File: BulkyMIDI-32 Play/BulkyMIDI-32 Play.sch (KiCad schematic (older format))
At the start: 45 parts, among them IC1 0.91_I2C_OLED, J1 DC IN, J10 MIDI IN (ALT), J11 MIDI OUT (ALT), J2 MIDI OUT, J3 MIDI IN, J4 Conn_Power, J5 MIDI THRU, J6 Play_Panel, M1 Mounting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

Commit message: Add schematic notes
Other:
- note added: "For a basic device with only MIDI OUT, the remaining\nMIDI components can be omitted. When building only\none MIDI IN circuit, you need to add R7 from the\nalternate circuit as well to avoid floating gate inputs."
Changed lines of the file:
@@
 Wire Bus Line
 	15050 7275 15050 8950
+Text Notes 9775 7375 0    50   ~ 0
+For a basic device with only MIDI OUT, the remaining\nMIDI components can be omitted. When building only\none MIDI IN circuit, you need to add R7 from the\nalternate circuit as well to avoid floating gate inputs.
 $EndSCHEMATC

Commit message: Build tweaks
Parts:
- U1: footprint Package_DIP:DIP-14_W7.62mm -> Package_DIP:DIP-14_W7.62mm_Socket_LongPads
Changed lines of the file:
@@
 F 0 "U1" H 6025 5775 50  0000 C CNN
 F 1 "74HCT14" H 6025 5700 50  0000 C CNN
-F 2 "Package_DIP:DIP-14_W7.62mm" H 6025 5500 50  0001 C CNN
+F 2 "Package_DIP:DIP-14_W7.62mm_Socket_LongPads" H 6025 5500 50  0001 C CNN
 F 3 "http://www.ti.com/lit/gpn/sn74HC14" H 6025 5500 50  0001 C CNN
 	4    6025 5500
@@
 F 0 "U1" H 5275 5875 50  0000 C CNN
 F 1 "74HCT14" H 5275 5800 50  0000 C CNN
-F 2 "Package_DIP:DIP-14_W7.62mm" H 5275 6050 50  0001 C CNN
+F 2 "Package_DIP:DIP-14_W7.62mm_Socket_LongPads" H 5275 6050 50  0001 C CNN
 F 3 "http://www.ti.com/lit/gpn/sn74HC14" H 5275 6050 50  0001 C CNN
 	5    5275 6050
@@
 F 0 "U1" H 6025 5875 50  0000 C CNN
 F 1 "74HCT14" H 6025 5800 50  0000 C CNN
-F 2 "Package_DIP:DIP-14_W7.62mm" H 6025 6050 50  0001 C CNN
+F 2 "Package_DIP:DIP-14_W7.62mm_Socket_LongPads" H 6025 6050 50  0001 C CNN
 F 3 "http://www.ti.com/lit/gpn/sn74HC14" H 6025 6050 50  0001 C CNN
 	6    6025 6050
@@
 F 0 "U1" V 10883 10250 50  0000 C CNN
 F 1 "74HCT14" V 10974 10250 50  0000 C CNN
-F 2 "Package_DIP:DIP-14_W7.62mm" H 11250 10250 50  0001 C CNN
+F 2 "Package_DIP:DIP-14_W7.62mm_Socket_LongPads" H 11250 10250 50  0001 C CNN
 F 3 "http://www.ti.com/lit/gpn/sn74HC14" H 11250 10250 50  0001 C CNN
 	7    11250 10250
@@
 F 0 "U1" H 6025 7300 50  0000 C CNN
 F 1 "74HCT14" H 6025 7225 50  0000 C CNN
-F 2 "Package_DIP:DIP-14_W7.62mm" H 6025 7475 50  0001 C CNN
+F 2 "Package_DIP:DIP-14_W7.62mm_Socket_LongPads" H 6025 7475 50  0001 C CNN
 F 3 "http://www.ti.com/lit/gpn/sn74HC14" H 6025 7475 50  0001 C CNN
 	2    6025 7475
@@
 F 0 "U1" H 5275 7300 50  0000 C CNN
 F 1 "74HCT14" H 5275 7225 50  0000 C CNN
-F 2 "Package_DIP:DIP-14_W7.62mm" H 5275 7475 50  0001 C CNN
+F 2 "Package_DIP:DIP-14_W7.62mm_Socket_LongPads" H 5275 7475 50  0001 C CNN
 F 3 "http://www.ti.com/lit/gpn/sn74HC14" H 5275 7475 50  0001 C CNN
 	1    5275 7475
@@
 Wire Wire Line
 	8050 7475 8125 7475
+Text Notes 9775 7375 0    50   ~ 0
+For a basic device with only MIDI OUT, the remaining\nMIDI components can be omitted. When building only\none MIDI IN circuit, you need to add R7 from the\nalternate circuit as well to avoid floating gate inputs.
 Wire Bus Line
 	15050 1100 15050 1275
@@
 Wire Bus Line
 	15050 7275 15050 8950
-Text Notes 9775 7375 0    50   ~ 0
-For a basic device with only MIDI OUT, the remaining\nMIDI components can be omitted. When building only\none MIDI IN circuit, you need to add R7 from the\nalternate circuit as well to avoid floating gate inputs.
 $EndSCHEMATC

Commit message: Forgotten gate
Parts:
- added unit 3 of U1
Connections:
- net GND: now also U1.5
- no-connect marks 18 -> 19
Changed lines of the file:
@@
 Text Notes 9775 7375 0    50   ~ 0
 For a basic device with only MIDI OUT, the remaining\nMIDI components can be omitted. When building only\none MIDI IN circuit, you need to add R7 from the\nalternate circuit as well to avoid floating gate inputs.
+$Comp
+L 74xx:74HC14 U1
+U 3 1 62B9B026
+P 6825 10600
+F 0 "U1" H 6825 10425 50  0000 C CNN
+F 1 "74HCT14" H 6825 10350 50  0000 C CNN
+F 2 "Package_DIP:DIP-14_W7.62mm_Socket_LongPads" H 6825 10600 50  0001 C CNN
+F 3 "http://www.ti.com/lit/gpn/sn74HC14" H 6825 10600 50  0001 C CNN
+	3    6825 10600
+	0    -1   -1   0
+$EndComp
+NoConn ~ 6825 10300
+$Comp
+L power:GND #PWR0121
+U 1 1 62BAE7B4
+P 6825 10900
+F 0 "#PWR0121" H 6825 10650 50  0001 C CNN
+F 1 "GND" H 6830 10727 50  0000 C CNN
+F 2 "" H 6825 10900 50  0001 C CNN
+F 3 "" H 6825 10900 50  0001 C CNN
+	1    6825 10900
+	1    0    0    -1
+$EndComp
 Wire Bus Line
 	15050 1100 15050 1275

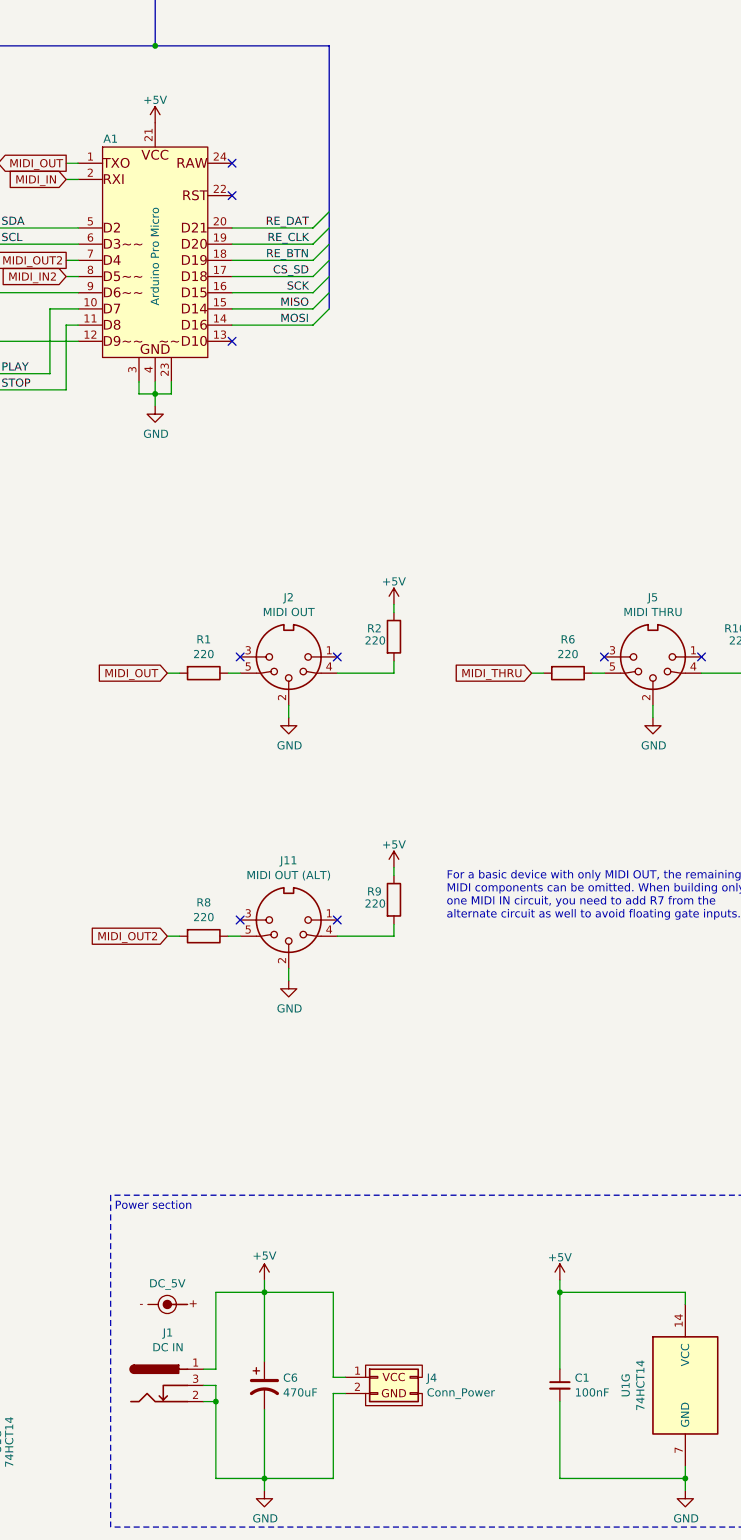
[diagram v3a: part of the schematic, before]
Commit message: Modules worked more reliably when run through the onboard regulator
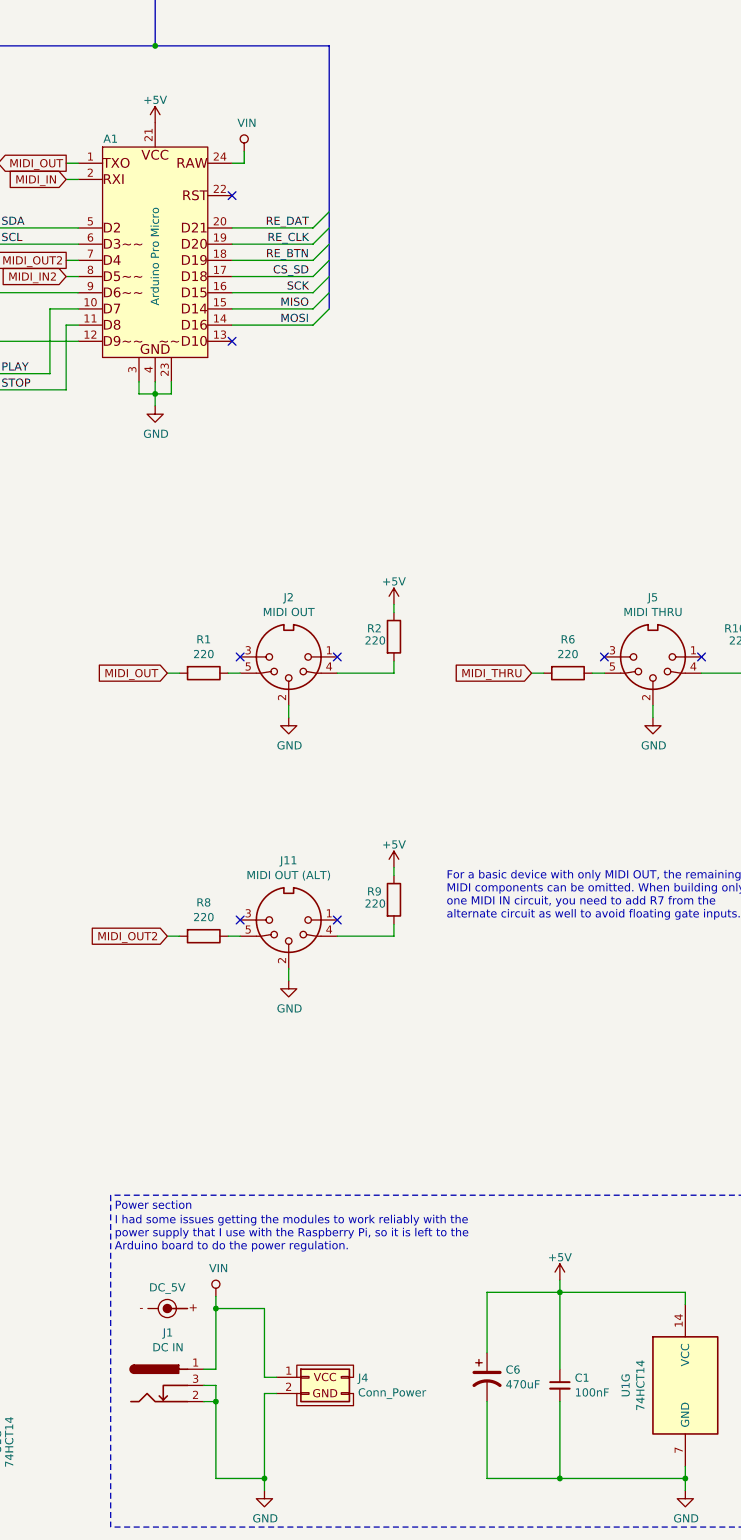
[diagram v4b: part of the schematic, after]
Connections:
- net +5V: no longer J1.1, J4.1 (VCC)
- net VIN: now reaches A1.24 (RAW)
- net VIN: now also J1.1, J4.1 (VCC)
- no-connect marks 19 -> 18
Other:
- note added: "I had some issues getting the modules to work reliably with the \npower supply that I use with the Raspberry Pi, so it is left to the\nArduino board to do the power regulation."
- moved on the sheet: C6, J4
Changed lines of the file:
@@
-$EndComp
-$Comp
-L power:+5V #PWR0106
-U 1 1 5E6B750D
-P 8650 9600
-F 0 "#PWR0106" H 8650 9450 50  0001 C CNN
-F 1 "+5V" H 8650 9750 50  0000 C CNN
-F 2 "" H 8650 9600 50  0001 C CNN
-F 3 "" H 8650 9600 50  0001 C CNN
-	1    8650 9600
-	1    0    0    -1
 $EndComp
 $Comp
@@
 L Device:CP1 C6
 U 1 1 5F9F946B
-P 8650 10250
-F 0 "C6" H 8765 10296 50  0000 L CNN
-F 1 "470uF" H 8765 10205 50  0000 L CNN
-F 2 "Capacitor_THT:CP_Radial_D8.0mm_P3.50mm" H 8650 10250 50  0001 C CNN
-F 3 "~" H 8650 10250 50  0001 C CNN
-	1    8650 10250
+P 10025 10200
+F 0 "C6" H 10140 10246 50  0000 L CNN
+F 1 "470uF" H 10140 10155 50  0000 L CNN
+F 2 "Capacitor_THT:CP_Radial_D8.0mm_P3.50mm" H 10025 10200 50  0001 C CNN
+F 3 "~" H 10025 10200 50  0001 C CNN
+	1    10025 10200
 	1    0    0    -1
 $EndComp
@@
 L BulkyMIDI:DC_5V SYM1
 U 1 1 623726BF
-P 8050 9750
-F 0 "SYM1" H 8050 9971 50  0001 C CNN
-F 1 "DC_5V" H 8050 9879 50  0000 C CNN
-F 2 "BulkyMIDI-32:PWR_Specification" H 7925 9850 50  0001 C CNN
-F 3 "" H 7925 9850 50  0001 C CNN
-	1    8050 9750
+P 8050 9775
+F 0 "SYM1" H 8050 9996 50  0001 C CNN
+F 1 "DC_5V" H 8050 9904 50  0000 C CNN
+F 2 "BulkyMIDI-32:PWR_Specification" H 7925 9875 50  0001 C CNN
+F 3 "" H 7925 9875 50  0001 C CNN
+	1    8050 9775
 	1    0    0    -1
 $EndComp
@@
 	1    0    0    -1
 $EndComp
-NoConn ~ 8450 2700
 NoConn ~ 8450 2900
 Text Label 7025 3100 0    50   ~ 0
@@
 L BulkyMIDI:Conn_Power J4
 U 1 1 62FD7887
-P 9350 10200
-F 0 "J4" H 9653 10196 50  0000 L CNN
-F 1 "Conn_Power" H 9653 10105 50  0000 L CNN
-F 2 "BulkyMIDI-32:Conn_Power" H 9350 10200 50  0001 C CNN
-F 3 "~" H 9350 10200 50  0001 C CNN
-	1    9350 10200
+P 8925 10200
+F 0 "J4" H 9228 10196 50  0000 L CNN
+F 1 "Conn_Power" H 9228 10105 50  0000 L CNN
+F 2 "BulkyMIDI-32:Conn_Power" H 8925 10200 50  0001 C CNN
+F 3 "~" H 8925 10200 50  0001 C CNN
+	1    8925 10200
 	1    0    0    -1
 $EndComp
@@
 Connection ~ 8350 10350
 Wire Wire Line
-	8650 9600 8650 9675
-Wire Wire Line
-	8650 9675 8350 9675
-Connection ~ 8650 9675
-Wire Wire Line
-	8350 9675 8350 10150
-Wire Wire Line
-	8650 9675 8650 10100
-Wire Wire Line
 	8650 10825 8350 10825
 Connection ~ 8650 10825
@@
 Wire Wire Line
 	8350 10350 8350 10825
-Wire Wire Line
-	8650 10400 8650 10825
 Wire Wire Line
 	11250 10825 11250 10900
@@
 	8425 7475 8500 7475
 Wire Wire Line
-	9150 10200 9075 10200
-Wire Wire Line
-	9075 10200 9075 9675
-Wire Wire Line
-	9075 9675 8650 9675
-Wire Wire Line
-	9150 10300 9075 10300
-Wire Wire Line
-	9075 10300 9075 10825
-Wire Wire Line
-	9075 10825 8650 10825
+	8725 10200 8650 10200
+Wire Wire Line
+	8650 10200 8650 9775
+Wire Wire Line
+	8725 10300 8650 10300
+Wire Wire Line
+	8650 10300 8650 10825
 Wire Notes Line
 	11675 9075 7700 9075
@@
 	1    0    0    -1
 $EndComp
+$Comp
+L barrel_jack:VIN #PWR0124
+U 1 1 62FF26B2
+P 8350 9700
+F 0 "#PWR0124" H 8350 9550 50  0001 C CNN
+F 1 "VIN" H 8367 9873 50  0000 C CNN
+F 2 "" H 8350 9700 50  0001 C CNN
+F 3 "" H 8350 9700 50  0001 C CNN
+	1    8350 9700
+	1    0    0    -1
+$EndComp
+$Comp
+L barrel_jack:VIN #PWR0125
+U 1 1 63007C95
+P 8525 2625
+F 0 "#PWR0125" H 8525 2475 50  0001 C CNN
+F 1 "VIN" H 8542 2798 50  0000 C CNN
+F 2 "" H 8525 2625 50  0001 C CNN
+F 3 "" H 8525 2625 50  0001 C CNN
+	1    8525 2625
+	1    0    0    -1
+$EndComp
+Wire Wire Line
+	8450 2700 8525 2700
+Wire Wire Line
+	8525 2700 8525 2625
+Text Notes 7725 9425 0    50   ~ 0
+I had some issues getting the modules to work reliably with the \npower supply that I use with the Raspberry Pi, so it is left to the\nArduino board to do the power regulation.
+Wire Wire Line
+	8350 9700 8350 9775
+Wire Wire Line
+	10025 9675 10475 9675
+Wire Wire Line
+	10025 9675 10025 10050
+Wire Wire Line
+	10475 10825 10025 10825
+Wire Wire Line
+	10025 10350 10025 10825
+Connection ~ 10475 10825
+Wire Wire Line
+	8650 9775 8350 9775
 Wire Bus Line
 	15050 1100 15050 1275
@@
 Wire Bus Line
 	15050 7275 15050 8950
+Connection ~ 8350 9775
+Wire Wire Line
+	8350 9775 8350 10150
 $EndSCHEMATC
